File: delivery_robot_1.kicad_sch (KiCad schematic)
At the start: 40 parts, among them J1 SWD, J10 Port C/D breakout, J11 IMU I2C (STEMMA QT), J12 IMU INT/RST, J13 Pi 5 UART, J14 Pi 5 power, J2 XT30PW-M, J4 BOOT0 jumper, J5 Conn_01x03_Pin, J6 MDD20A PWM1/DIR1/GND, J7 Motor1 encoder, J8 Port A breakout, J9 Port B breakout, SW1 RESET, U1 STM32F091RCTx, Y3 8MHz

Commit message: Add second 6 A buck and split Pi and GPIO blocks into sheets
Duplicate the 12 V to 5 V, 6 A TPSM63606 buck as an independent
sheet (Buck_5V_6A_AUX, U5, C28-C33, R14-R16) and rename the two
outputs so they can't be confused:
- +5V, 6A PI: the existing buck (U2), feeding the Pi 5 via F2/J14
- +5V, 6A AUX: the new buck (U5), no loads assigned yet

Move the Raspberry Pi 5 UART (J13, R12/R13) and power output
(F2, J14, TP1/TP2) into Pi5_Interface.kicad_sch, with sheet pins
USART2_TX, USART2_RX and VIN_5V (from +5V, 6A PI). PI_TXD/PI_RXD
become local labels inside the sheet.

Move the J8-J10 GPIO breakout headers into GPIO_Breakout.kicad_sch.
They keep their global labels, so the block has no sheet pins.

The split leaves connectivity unchanged: the netlist has the same
86 nets and 75 components as before. Fix the stale UART note that
referred to the removed U5 ESD array. Update README and
docs/power-supply.md, and include schematic layout changes made
in KiCad.

Co-Authored-By: Claude Opus 5.5 <noreply@anthropic.com>
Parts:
- removed F2: 7.5A / 32VDC, Fuse:Fuseholder_Blade_Mini_Keystone_3568, symbol Device:Fuse
- removed J10: Port C/D breakout, Connector_PinHeader_2.54mm:PinHeader_1x18_P2.54mm_Vertical, symbol Connector:Conn_01x18_Pin
- removed J13: Pi 5 UART, TerminalBlock_Phoenix:TerminalBlock_Phoenix_MKDS-1,5-3_1x03_P5.00mm_Horizontal, symbol Connector:Screw_Terminal_01x03
- removed J14: Pi 5 power, TerminalBlock_Phoenix:TerminalBlock_Phoenix_MKDS-1,5-2_1x02_P5.00mm_Horizontal, symbol Connector:Screw_Terminal_01x02
- removed J8: Port A breakout, Connector_PinHeader_2.54mm:PinHeader_1x13_P2.54mm_Vertical, symbol Connector:Conn_01x13_Pin
- removed J9: Port B breakout, Connector_PinHeader_2.54mm:PinHeader_1x15_P2.54mm_Vertical, symbol Connector:Conn_01x15_Pin
- removed R12, R13: 100, Resistor_SMD:R_0805_2012Metric, symbol Device:R
- removed TP1: +5V, 6A, TestPoint:TestPoint_Keystone_5000-5004_Miniature, symbol Connector:TestPoint
- removed TP2: PI_5V, TestPoint:TestPoint_Keystone_5000-5004_Miniature, symbol Connector:TestPoint
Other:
- sheet Buck 12V-5V 6A renamed Buck 12V-5V 6A PI
- added sheet Buck 12V-5V 6A AUX (Buck_5V_6A_AUX.kicad_sch)
- added sheet MCU GPIO Breakout (GPIO_Breakout.kicad_sch)
- added sheet Pi 5 Interface (Pi5_Interface.kicad_sch)
- note added: "12 V to 5 V / 6 A buck - U2 (TPSM63606) Output is the +5V, 6A PI net (feeds the Pi via F2/J14)"
- note added: "J13 Pi UART (R12/R13 100R) J14 Pi power via F2 isolation fuse"
- note added: "J8-J10: 2.54 mm headers for every spare STM32 pin. Connected by global labels, so the block has no sheet pins."
- note removed: "12 V to 5 V / 6 A buck - U2 (TPSM63606) Output is the separate +5V, 6A net"
- note removed: "Bring-up: F2 out, check TP1; fit F2, load-test J14; then connect the Pi. 5-6 A path"
- note removed: "J13 1 <- Pi GPIO14 TXD (header pin 8) J13 2 -> Pi GPIO15 RXD (header pin 10) J13 3 = GND (Pi header pin 6); 3.3 V logic R12/R13 near U1, U5 ESD near J13"
- note removed: "MCU GPIO breakout - 2.54 mm male pin headers (J8 port A, J9 port B, J10 ports C/D) Every spare STM32 pin is brought out by global label; the last pin of each header is GND."
- note removed: "Pi 5 power: +5V, 6A -> F2 isolation fuse -> J14 USB-C pigtail"
- note removed: "Raspberry Pi 5 UART (USART2, PA2 TX / PA3 RX)"

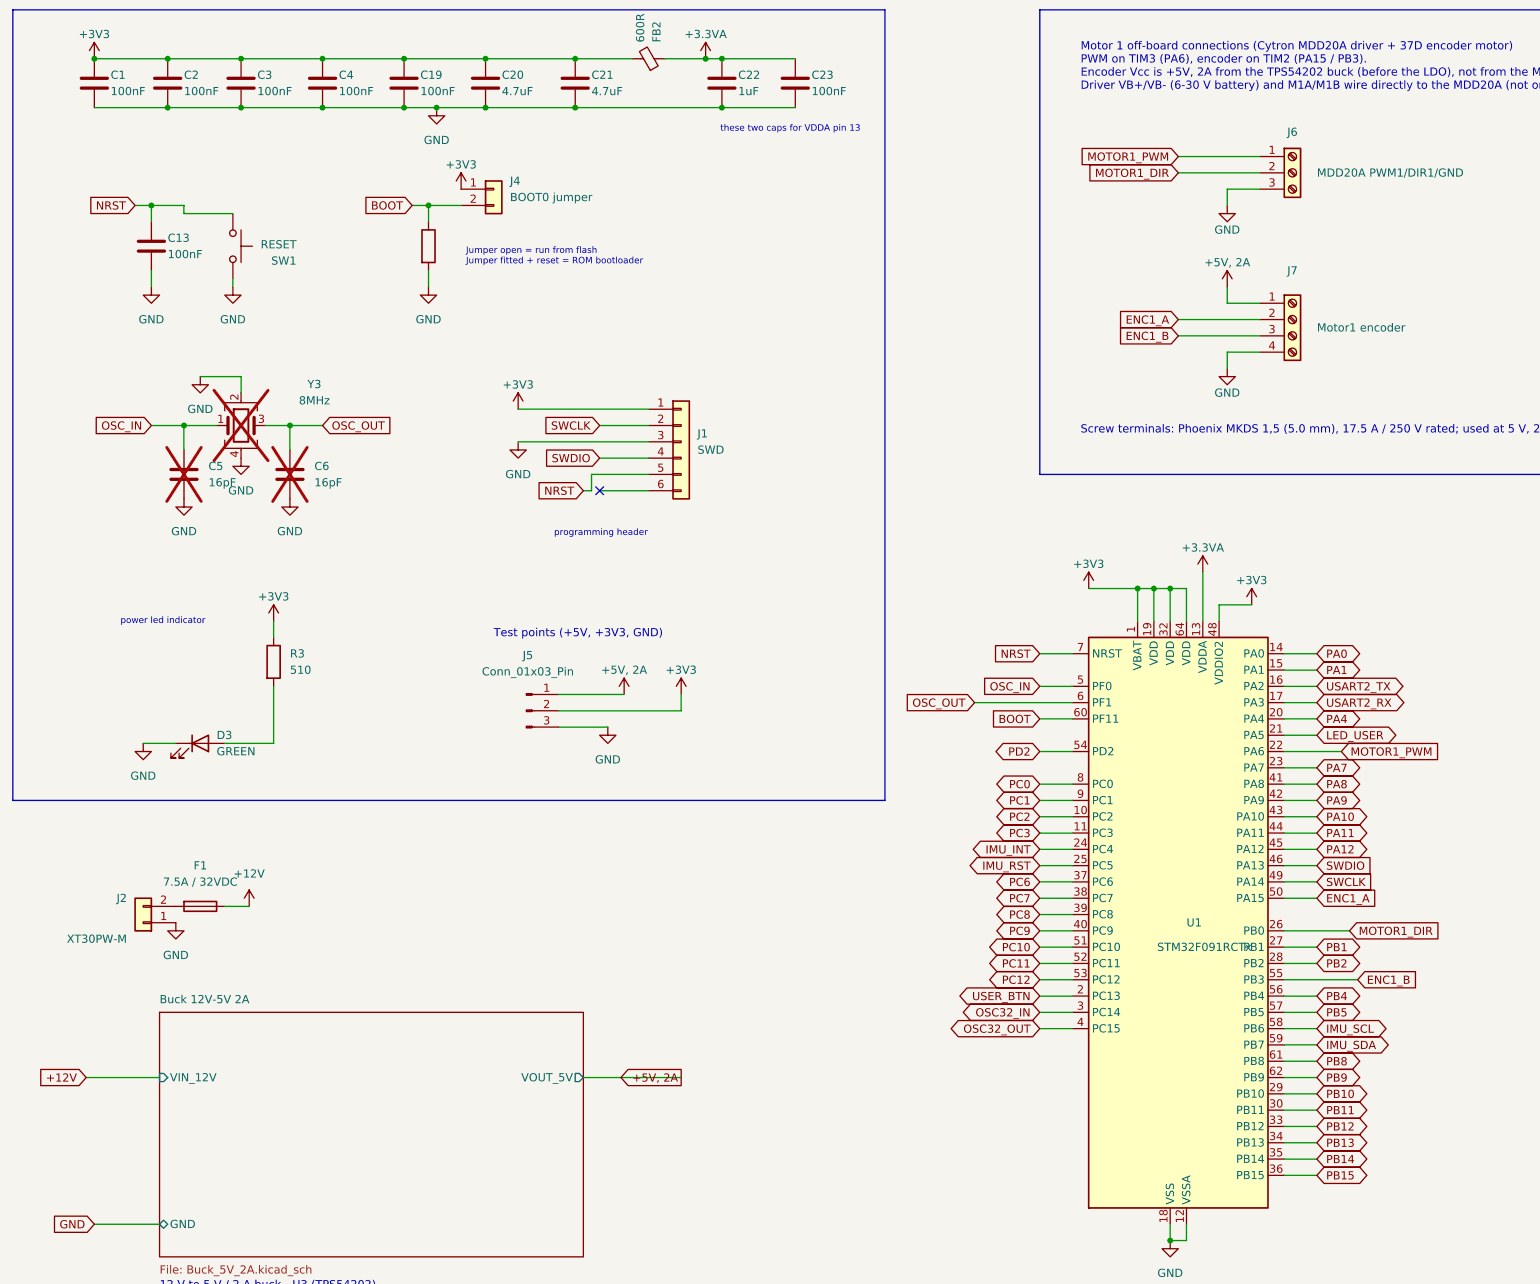
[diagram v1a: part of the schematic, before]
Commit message: Add power-rail and debug LEDs and an NRST pull-up
New Power_Indicators.kicad_sch sheet (page 8):
- One green LED per rail (Lite-On LTST-C190KGKT, 0603, 2.0 V typ):
  +12V D4/R17 4.7k, +5V 6A PI D5/R18 1.5k, +5V 6A AUX D6/R19 1.5k,
  +5V 2A D7/R20 1.5k, +3V3 D3/R3 510R (moved from the root sheet).
  About 2-2.7 mA each; worst-case resistor dissipation 34 mW (R17).
- Four yellow active-high STM32 debug LEDs (LTST-C190KSKT, 680R,
  1.8 mA): D8 LED_USER (PA5), D9 LED_PI_LINK (PB12), D10 LED_IMU
  (PB13), D11 LED_MOTOR (PB14). PB12-PB14 global labels are renamed
  at U1 and on the J9 breakout header.
- Uses the current KiCad Device:LED symbol, clearing the stale
  lib_symbol_mismatch warning on D3.

Add R25, a 10k 0805 pull-up from NRST to +3V3, alongside C13 and the
reset button, to keep the reset line firm against motor and
regulator noise.

Co-Authored-By: Claude Opus 5.5 <noreply@anthropic.com>
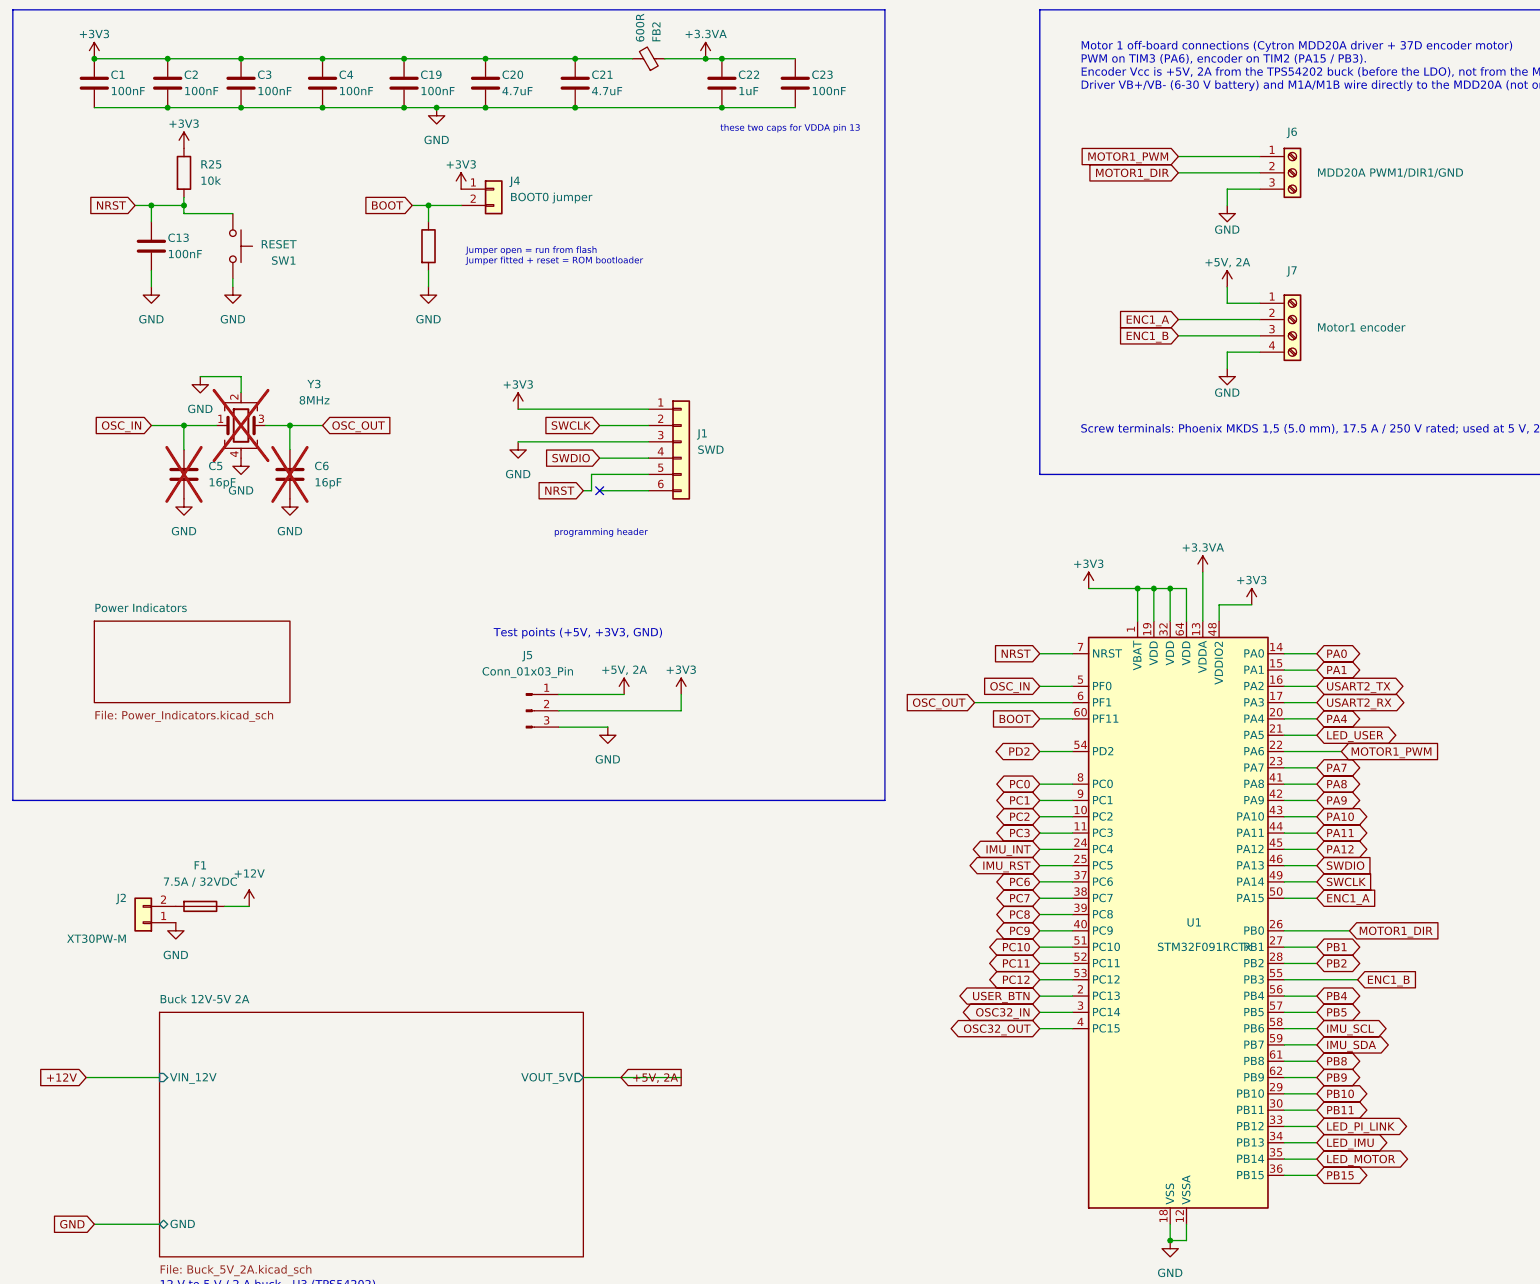
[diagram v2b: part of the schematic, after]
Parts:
- removed D3: GREEN, LED_SMD:LED_0603_1608Metric, symbol Device:LED
- removed R3: 510, Resistor_SMD:R_0805_2012Metric, symbol Device:R
- added R25: 10k, Resistor_SMD:R_0805_2012Metric, symbol Device:R
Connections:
- net +3V3: now also R25.1
- net NRST: now also R25.2
- net PB12 renamed LED_PI_LINK
- net PB13 renamed LED_IMU
- net PB14 renamed LED_MOTOR
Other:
- added sheet Power Indicators (Power_Indicators.kicad_sch)
- note removed: "power led indicator"
